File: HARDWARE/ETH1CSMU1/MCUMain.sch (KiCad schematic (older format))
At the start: 31 parts, among them J701 Conn_02x05, U701 STM32F746ZETx, U702 24LC08, X701 CRYSTAL_4PIN

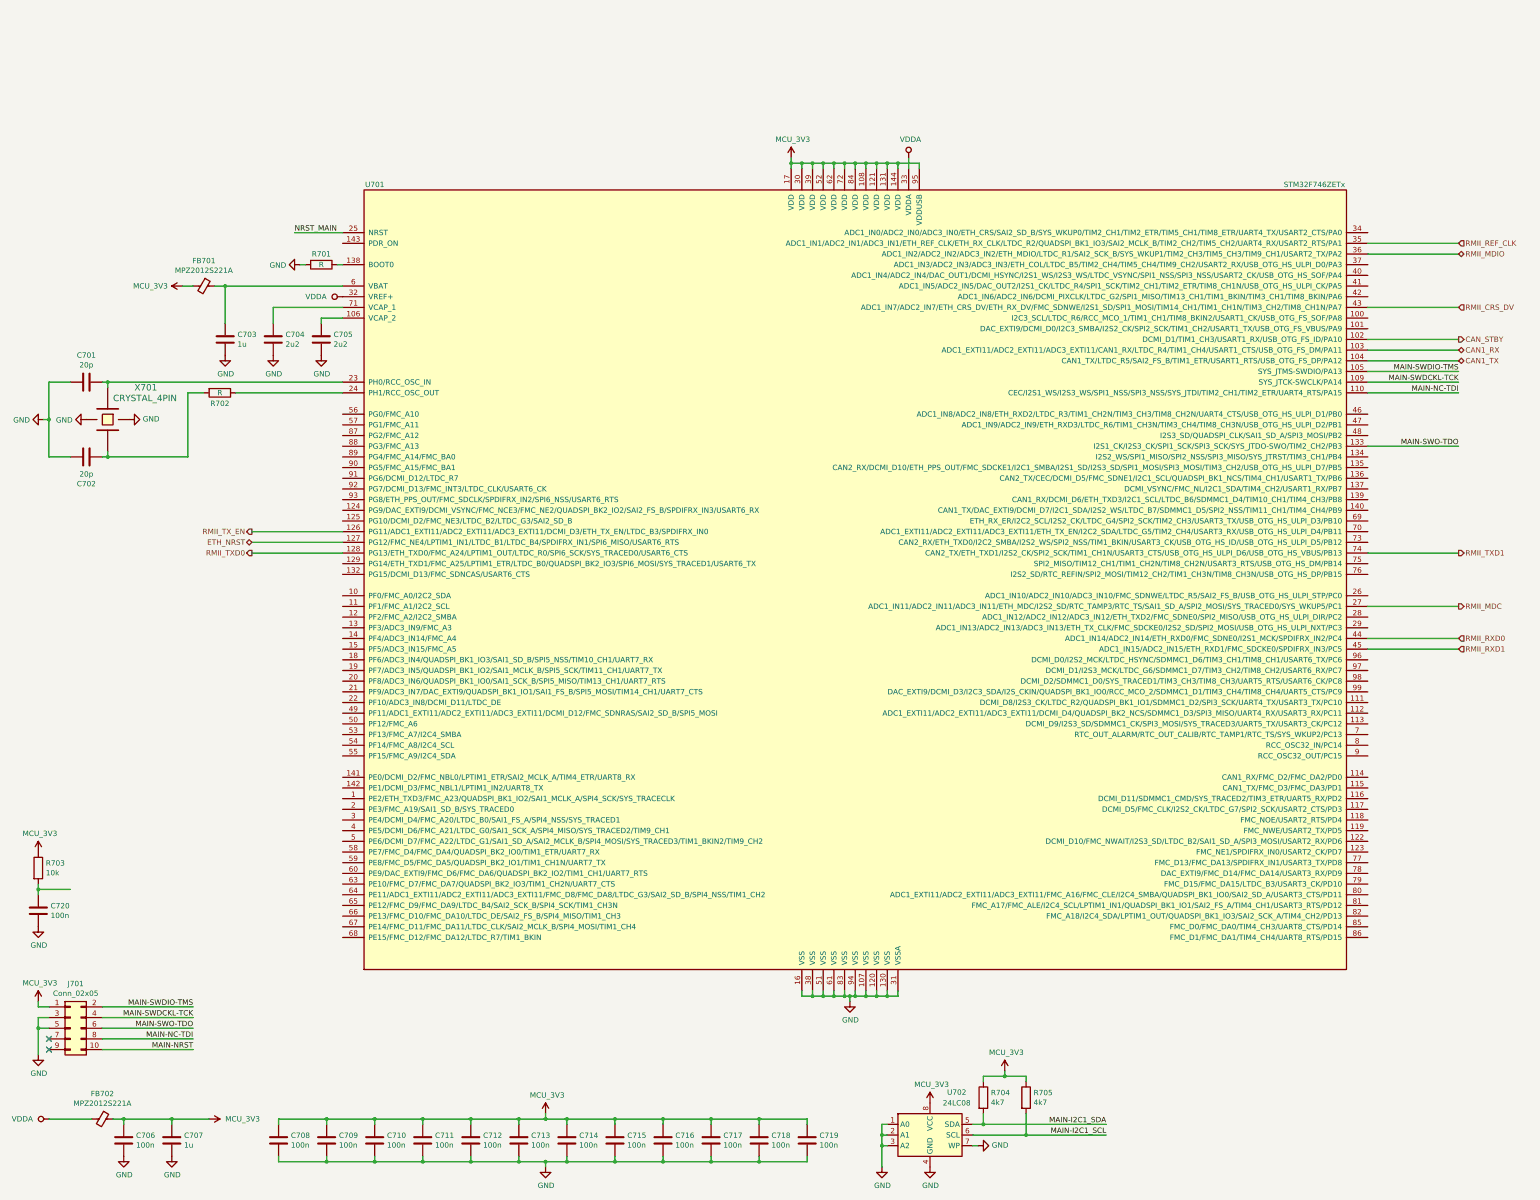
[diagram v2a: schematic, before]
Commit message: Power schematic
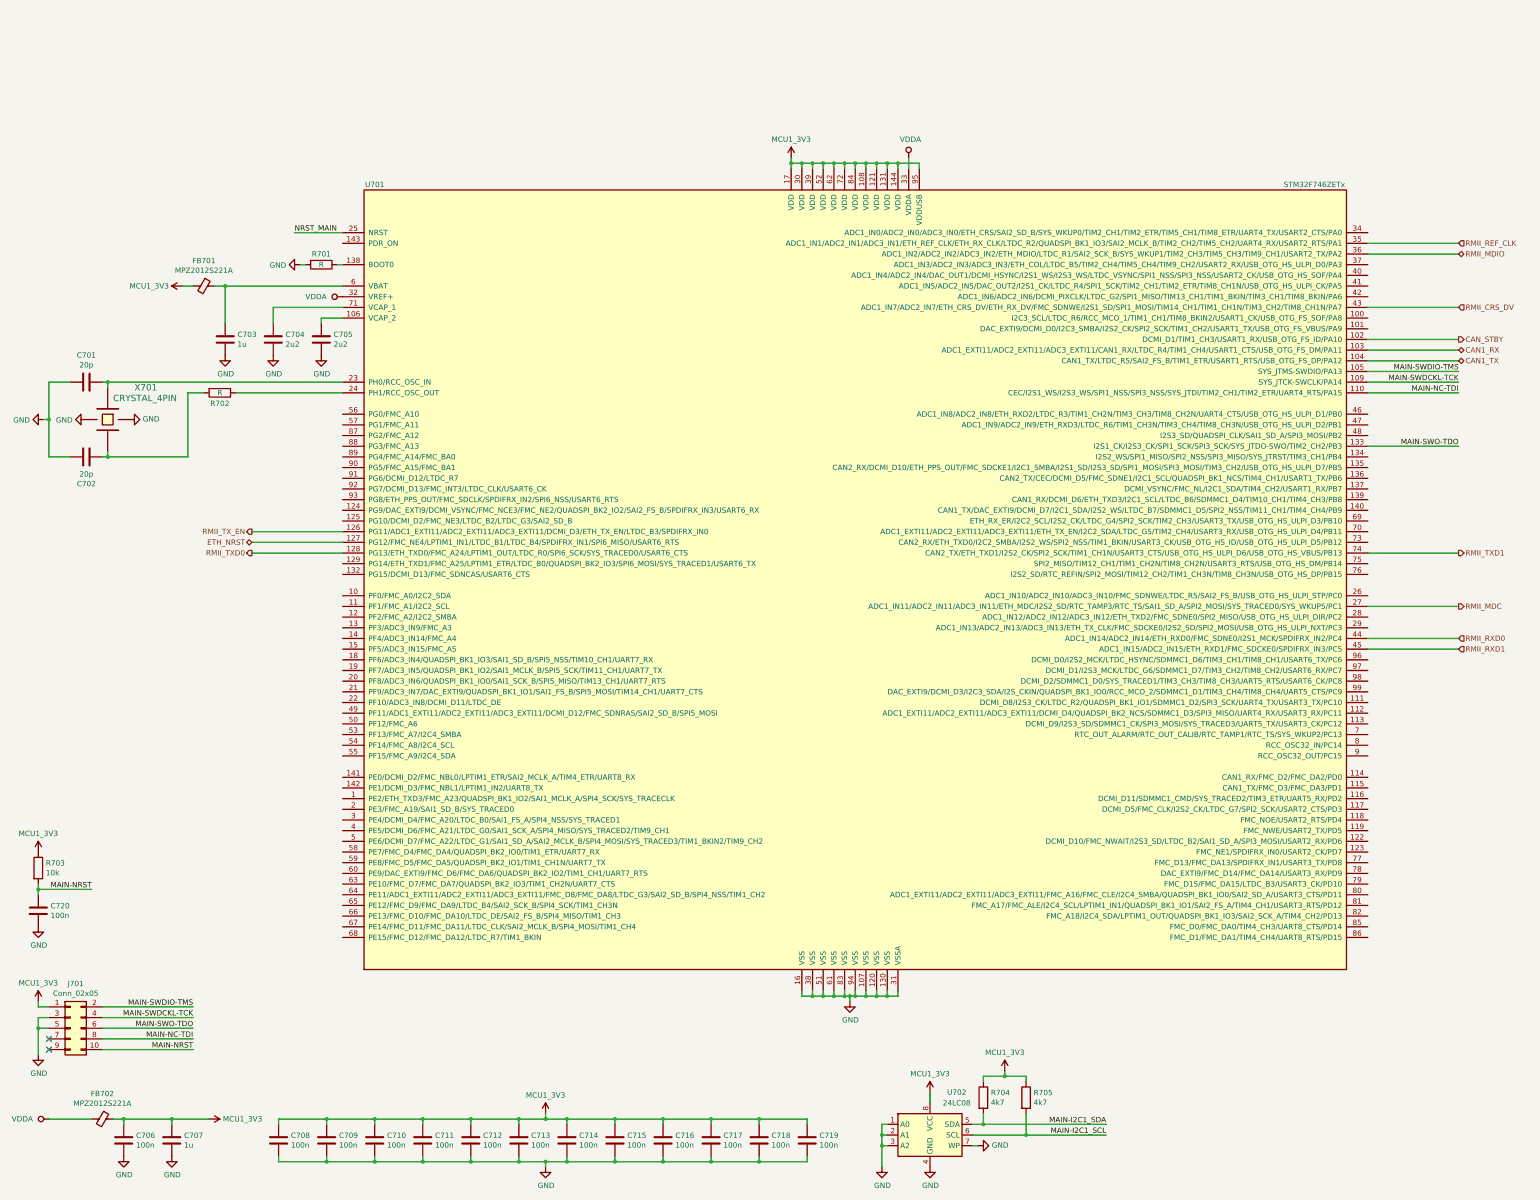
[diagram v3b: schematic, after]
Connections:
- net MAIN-NRST: now also C720.1, R703.2
- net MCU_3V3 renamed MCU1_3V3
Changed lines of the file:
@@
 $Descr A3 16535 11693
 encoding utf-8
-Sheet 7 12
+Sheet 7 13
 Title ""
 Date ""
@@
 F 3 "http://www.st.com/st-web-ui/static/active/en/resource/technical/document/datasheet/DM00166116.pdf" H 8450 5500 50  0001 C CNN
 	1    8450 5500
-	1    0    0    -1
-$EndComp
-$Comp
-L power_local:MCU_3V3 #PWR0702
-U 1 1 5BE1264D
-P 7850 1500
-F 0 "#PWR0702" H 7850 1350 50  0001 C CNN
-F 1 "MCU_3V3" H 7865 1673 50  0000 C CNN
-F 2 "" H 7850 1500 50  0000 C CNN
-F 3 "" H 7850 1500 50  0000 C CNN
-	1    7850 1500
 	1    0    0    -1
 $EndComp
@@
 Connection ~ 8850 1550
 $Comp
-L power_local:MCU_3V3 #PWR0703
-U 1 1 5BEBBE17
-P 2150 2700
-F 0 "#PWR0703" H 2150 2550 50  0001 C CNN
-F 1 "MCU_3V3" V 2150 3000 50  0000 C CNN
-F 2 "" H 2150 2700 50  0000 C CNN
-F 3 "" H 2150 2700 50  0000 C CNN
-	1    2150 2700
-	0    -1   -1   0
-$EndComp
-$Comp
 L Device:C C703
 U 1 1 5BEBD2EF
@@
 Connection ~ 2050 10500
 $Comp
-L power_local:MCU_3V3 #PWR0711
-U 1 1 5BEE572D
-P 2400 10500
-F 0 "#PWR0711" H 2400 10350 50  0001 C CNN
-F 1 "MCU_3V3" V 2400 10650 50  0000 L CNN
-F 2 "" H 2400 10500 50  0000 C CNN
-F 3 "" H 2400 10500 50  0000 C CNN
-	1    2400 10500
-	0    1    1    0
-$EndComp
-$Comp
 L power:VDDA #PWR0712
 U 1 1 5BEE8DB0
@@
 Wire Wire Line
 	5550 10900 5300 10900
-$Comp
-L power_local:MCU_3V3 #PWR0714
-U 1 1 5BF46B64
-P 5550 10450
-F 0 "#PWR0714" H 5550 10300 50  0001 C CNN
-F 1 "MCU_3V3" H 5565 10623 50  0000 C CNN
-F 2 "" H 5550 10450 50  0000 C CNN
-F 3 "" H 5550 10450 50  0000 C CNN
-	1    5550 10450
-	1    0    0    -1
-$EndComp
 Wire Wire Line
 	5550 10450 5550 10500
@@
 	1    0    0    -1
 $EndComp
-Wire Wire Line
-	800  8350 1100 8350
-$Comp
-L power_local:MCU_3V3 #PWR?
-U 1 1 5C07DDC6
-P 800 8000
-AR Path="/5BE0F4FE/5C07DDC6" Ref="#PWR?"  Part="1"
-AR Path="/5BE4235D/5C07DDC6" Ref="#PWR0716"  Part="1"
-F 0 "#PWR0716" H 800 7850 50  0001 C CNN
-F 1 "MCU_3V3" H 815 8173 50  0000 C CNN
-F 2 "" H 800 8000 50  0000 C CNN
-F 3 "" H 800 8000 50  0000 C CNN
-	1    800  8000
-	1    0    0    -1
-$EndComp
 $Comp
 L Connector_Generic:Conn_02x05_Odd_Even J?
@@
 F 3 "" H 800 9900 50  0001 C CNN
 	1    800  9900
-	1    0    0    -1
-$EndComp
-$Comp
-L power_local:MCU_3V3 #PWR?
-U 1 1 5BF91DF4
-P 800 9400
-AR Path="/5BE0F4FE/5BF91DF4" Ref="#PWR?"  Part="1"
-AR Path="/5BE4235D/5BF91DF4" Ref="#PWR0718"  Part="1"
-F 0 "#PWR0718" H 800 9250 50  0001 C CNN
-F 1 "MCU_3V3" H 815 9573 50  0000 C CNN
-F 2 "" H 800 9400 50  0000 C CNN
-F 3 "" H 800 9400 50  0000 C CNN
-	1    800  9400
 	1    0    0    -1
 $EndComp
@@
 	0    -1   -1   0
 $EndComp
-$Comp
-L power_local:MCU_3V3 #PWR?
-U 1 1 5C0622E5
-P 9150 10350
-AR Path="/5BE0F4FE/5C0622E5" Ref="#PWR?"  Part="1"
-AR Path="/5BE4235D/5C0622E5" Ref="#PWR0721"  Part="1"
-F 0 "#PWR0721" H 9150 10200 50  0001 C CNN
-F 1 "MCU_3V3" H 9165 10523 50  0000 C CNN
-F 2 "" H 9150 10350 50  0000 C CNN
-F 3 "" H 9150 10350 50  0000 C CNN
-	1    9150 10350
-	1    0    0    -1
-$EndComp
-$Comp
-L power_local:MCU_3V3 #PWR?
-U 1 1 5C0622EB
-P 9850 10050
-AR Path="/5BE0F4FE/5C0622EB" Ref="#PWR?"  Part="1"
-AR Path="/5BE4235D/5C0622EB" Ref="#PWR0724"  Part="1"
-F 0 "#PWR0724" H 9850 9900 50  0001 C CNN
-F 1 "MCU_3V3" H 9865 10223 50  0000 C CNN
-F 2 "" H 9850 10050 50  0000 C CNN
-F 3 "" H 9850 10050 50  0000 C CNN
-	1    9850 10050
-	1    0    0    -1
-$EndComp
 Wire Wire Line
 	2650 3700 3650 3700
@@
 Text HLabel 14100 3200 2    50   Output ~ 0
 CAN_STBY
+Text Label 1300 8350 2    50   ~ 0
+MAIN-NRST
+Wire Wire Line
+	800  8350 1300 8350
+$Comp
+L power_local:MCU1_3V3 #PWR?
+U 1 1 5C41AD37
+P 800 8000
+F 0 "#PWR?" H 800 7900 50  0001 C CNN
+F 1 "MCU1_3V3" H 800 8173 50  0000 C CNN
+F 2 "" H 800 8000 50  0000 C CNN
+F 3 "" H 800 8000 50  0000 C CNN
+	1    800  8000
+	1    0    0    -1
+$EndComp
+$Comp
+L power_local:MCU1_3V3 #PWR?
+U 1 1 5C41AE03
+P 800 9400
+F 0 "#PWR?" H 800 9300 50  0001 C CNN
+F 1 "MCU1_3V3" H 800 9573 50  0000 C CNN
+F 2 "" H 800 9400 50  0000 C CNN
+F 3 "" H 800 9400 50  0000 C CNN
+	1    800  9400
+	1    0    0    -1
+$EndComp
+$Comp
+L power_local:MCU1_3V3 #PWR?
+U 1 1 5C41AF63
+P 5550 10450
+F 0 "#PWR?" H 5550 10350 50  0001 C CNN
+F 1 "MCU1_3V3" H 5550 10623 50  0000 C CNN
+F 2 "" H 5550 10450 50  0000 C CNN
+F 3 "" H 5550 10450 50  0000 C CNN
+	1    5550 10450
+	1    0    0    -1
+$EndComp
+$Comp
+L power_local:MCU1_3V3 #PWR?
+U 1 1 5C41B120
+P 9850 10050
+F 0 "#PWR?" H 9850 9950 50  0001 C CNN
+F 1 "MCU1_3V3" H 9850 10223 50  0000 C CNN
+F 2 "" H 9850 10050 50  0000 C CNN
+F 3 "" H 9850 10050 50  0000 C CNN
+	1    9850 10050
+	1    0    0    -1
+$EndComp
+$Comp
+L power_local:MCU1_3V3 #PWR?
+U 1 1 5C41B280
+P 7850 1500
+F 0 "#PWR?" H 7850 1400 50  0001 C CNN
+F 1 "MCU1_3V3" H 7850 1673 50  0000 C CNN
+F 2 "" H 7850 1500 50  0000 C CNN
+F 3 "" H 7850 1500 50  0000 C CNN
+	1    7850 1500
+	1    0    0    -1
+$EndComp
+$Comp
+L power_local:MCU1_3V3 #PWR?
+U 1 1 5C41B516
+P 2150 2700
+F 0 "#PWR?" H 2150 2600 50  0001 C CNN
+F 1 "MCU1_3V3" V 2150 2827 50  0000 L CNN
+F 2 "" H 2150 2700 50  0000 C CNN
+F 3 "" H 2150 2700 50  0000 C CNN
+	1    2150 2700
+	0    -1   -1   0
+$EndComp
+$Comp
+L power_local:MCU1_3V3 #PWR?
+U 1 1 5C41D671
+P 9150 10250
+F 0 "#PWR?" H 9150 10150 50  0001 C CNN
+F 1 "MCU1_3V3" H 9150 10423 50  0000 C CNN
+F 2 "" H 9150 10250 50  0000 C CNN
+F 3 "" H 9150 10250 50  0000 C CNN
+	1    9150 10250
+	1    0    0    -1
+$EndComp
+Wire Wire Line
+	9150 10250 9150 10350
+$Comp
+L power_local:MCU1_3V3 #PWR?
+U 1 1 5C4345B7
+P 2400 10500
+F 0 "#PWR?" H 2400 10400 50  0001 C CNN
+F 1 "MCU1_3V3" V 2400 10628 50  0000 L CNN
+F 2 "" H 2400 10500 50  0000 C CNN
+F 3 "" H 2400 10500 50  0000 C CNN
+	1    2400 10500
+	0    1    1    0
+$EndComp
 $EndSCHEMATC

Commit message: Footprints
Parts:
- C701, C702: footprint (none) -> Capacitors_SMD:C_0603
- C706: footprint (none) -> SMD:C_0603_Symbol1
- J701: footprint (none) -> Pin_Headers:Pin_Header_Straight_2x05_Pitch1.27mm
- U701: footprint (none) -> SMD:TQFP-144
- U702: footprint (none) -> Housings_SSOP:MSOP-8_3x3mm_Pitch0.65mm
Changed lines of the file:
@@
 F 0 "U701" H 3950 9250 50  0000 C CNN
 F 1 "STM32F746ZETx" H 12750 9250 50  0000 C CNN
-F 2 "" H 13050 9175 50  0001 R TNN
+F 2 "SMD:TQFP-144" H 13050 9175 50  0001 R TNN
 F 3 "http://www.st.com/st-web-ui/static/active/en/resource/technical/document/datasheet/DM00166116.pdf" H 8450 5500 50  0001 C CNN
 	1    8450 5500
@@
 F 0 "C701" V 998 3600 50  0000 C CNN
 F 1 "20p" V 1089 3600 50  0000 C CNN
-F 2 "" H 1288 3450 50  0001 C CNN
+F 2 "Capacitors_SMD:C_0603" H 1288 3450 50  0001 C CNN
 F 3 "~" H 1250 3600 50  0001 C CNN
 	1    1250 3600
@@
 F 0 "C702" V 1502 4300 50  0000 C CNN
 F 1 "20p" V 1411 4300 50  0000 C CNN
-F 2 "" H 1288 4150 50  0001 C CNN
+F 2 "Capacitors_SMD:C_0603" H 1288 4150 50  0001 C CNN
 F 3 "~" H 1250 4300 50  0001 C CNN
 	1    1250 4300
@@
 F 0 "C706" H 1715 10746 50  0000 L CNN
 F 1 "100n" H 1715 10655 50  0000 L CNN
-F 2 "" H 1638 10550 50  0001 C CNN
+F 2 "SMD:C_0603_Symbol1" H 1638 10550 50  0001 C CNN
 F 3 "~" H 1600 10700 50  0001 C CNN
 	1    1600 10700
@@
 F 0 "J701" H 1150 10067 50  0000 C CNN
 F 1 "Conn_02x05" H 1150 9976 50  0000 C CNN
-F 2 "" H 1100 9650 50  0001 C CNN
+F 2 "Pin_Headers:Pin_Header_Straight_2x05_Pitch1.27mm" H 1100 9650 50  0001 C CNN
 F 3 "~" H 1100 9650 50  0001 C CNN
 	1    1100 9650
@@
 F 0 "U702" H 9400 11050 50  0000 C CNN
 F 1 "24LC08" H 9400 10950 50  0000 C CNN
-F 2 "" H 9150 10650 50  0001 C CNN
+F 2 "Housings_SSOP:MSOP-8_3x3mm_Pitch0.65mm" H 9150 10650 50  0001 C CNN
 F 3 "http://ww1.microchip.com/downloads/en/DeviceDoc/21710J.pdf" H 9150 10650 50  0001 C CNN
 	1    9150 10650
@@
 	800  8350 1300 8350
 $Comp
-L power_local:MCU1_3V3 #PWR?
+L power_local:MCU1_3V3 #PWR0123
 U 1 1 5C41AD37
 P 800 8000
-F 0 "#PWR?" H 800 7900 50  0001 C CNN
+F 0 "#PWR0123" H 800 7900 50  0001 C CNN
 F 1 "MCU1_3V3" H 800 8173 50  0000 C CNN
 F 2 "" H 800 8000 50  0000 C CNN
@@
 $EndComp
 $Comp
-L power_local:MCU1_3V3 #PWR?
+L power_local:MCU1_3V3 #PWR0124
 U 1 1 5C41AE03
 P 800 9400
-F 0 "#PWR?" H 800 9300 50  0001 C CNN
+F 0 "#PWR0124" H 800 9300 50  0001 C CNN
 F 1 "MCU1_3V3" H 800 9573 50  0000 C CNN
 F 2 "" H 800 9400 50  0000 C CNN
@@
 $EndComp
 $Comp
-L power_local:MCU1_3V3 #PWR?
+L power_local:MCU1_3V3 #PWR0125
 U 1 1 5C41AF63
 P 5550 10450
-F 0 "#PWR?" H 5550 10350 50  0001 C CNN
+F 0 "#PWR0125" H 5550 10350 50  0001 C CNN
 F 1 "MCU1_3V3" H 5550 10623 50  0000 C CNN
 F 2 "" H 5550 10450 50  0000 C CNN
@@
 $EndComp
 $Comp
-L power_local:MCU1_3V3 #PWR?
+L power_local:MCU1_3V3 #PWR0126
 U 1 1 5C41B120
 P 9850 10050
-F 0 "#PWR?" H 9850 9950 50  0001 C CNN
+F 0 "#PWR0126" H 9850 9950 50  0001 C CNN
 F 1 "MCU1_3V3" H 9850 10223 50  0000 C CNN
 F 2 "" H 9850 10050 50  0000 C CNN
@@
 $EndComp
 $Comp
-L power_local:MCU1_3V3 #PWR?
+L power_local:MCU1_3V3 #PWR0127
 U 1 1 5C41B280
 P 7850 1500
-F 0 "#PWR?" H 7850 1400 50  0001 C CNN
+F 0 "#PWR0127" H 7850 1400 50  0001 C CNN
 F 1 "MCU1_3V3" H 7850 1673 50  0000 C CNN
 F 2 "" H 7850 1500 50  0000 C CNN
@@
 $EndComp
 $Comp
-L power_local:MCU1_3V3 #PWR?
+L power_local:MCU1_3V3 #PWR0128
 U 1 1 5C41B516
 P 2150 2700
-F 0 "#PWR?" H 2150 2600 50  0001 C CNN
+F 0 "#PWR0128" H 2150 2600 50  0001 C CNN
 F 1 "MCU1_3V3" V 2150 2827 50  0000 L CNN
 F 2 "" H 2150 2700 50  0000 C CNN
@@
 $EndComp
 $Comp
-L power_local:MCU1_3V3 #PWR?
+L power_local:MCU1_3V3 #PWR0129
 U 1 1 5C41D671
 P 9150 10250
-F 0 "#PWR?" H 9150 10150 50  0001 C CNN
+F 0 "#PWR0129" H 9150 10150 50  0001 C CNN
 F 1 "MCU1_3V3" H 9150 10423 50  0000 C CNN
 F 2 "" H 9150 10250 50  0000 C CNN
@@
 	9150 10250 9150 10350
 $Comp
-L power_local:MCU1_3V3 #PWR?
+L power_local:MCU1_3V3 #PWR0130
 U 1 1 5C4345B7
 P 2400 10500
-F 0 "#PWR?" H 2400 10400 50  0001 C CNN
+F 0 "#PWR0130" H 2400 10400 50  0001 C CNN
 F 1 "MCU1_3V3" V 2400 10628 50  0000 L CNN
 F 2 "" H 2400 10500 50  0000 C CNN

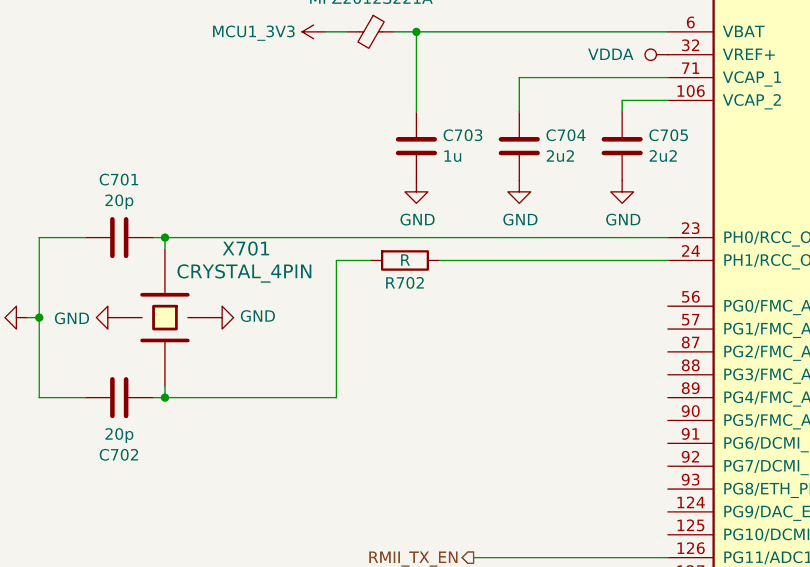
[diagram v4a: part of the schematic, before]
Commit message: Footprint selection
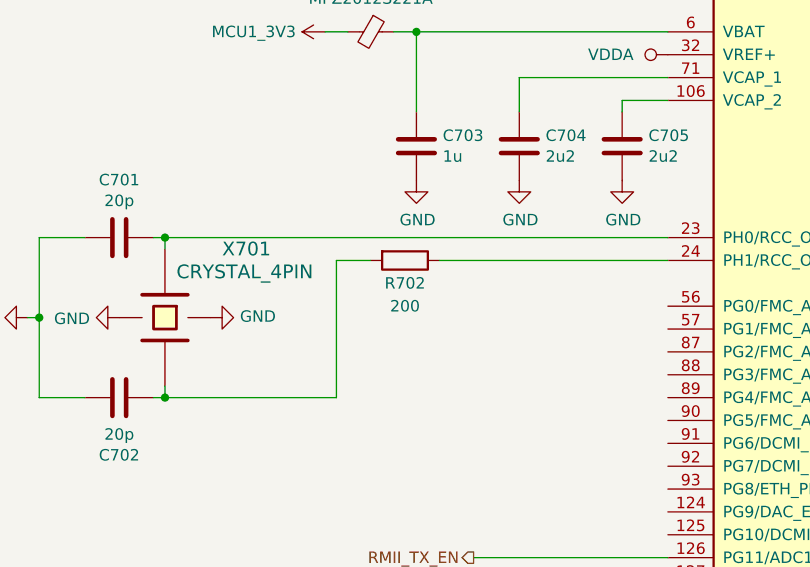
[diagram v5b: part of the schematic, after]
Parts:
- R702: value R -> 200
- R704, R705: footprint (none) -> SMD:R_0603_Symbol6
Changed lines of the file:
@@
 P 2500 3700
 F 0 "R702" V 2600 3700 50  0000 C CNN
-F 1 "R" V 2500 3700 50  0000 C CNN
+F 1 "200" V 2700 3700 50  0000 C CNN
 F 2 "" V 2430 3700 50  0001 C CNN
 F 3 "~" H 2500 3700 50  0001 C CNN
@@
 F 0 "R704" H 9720 10346 50  0000 L CNN
 F 1 "4k7" H 9720 10255 50  0000 L CNN
-F 2 "" V 9580 10300 50  0001 C CNN
+F 2 "SMD:R_0603_Symbol6" V 9580 10300 50  0001 C CNN
 F 3 "~" H 9650 10300 50  0001 C CNN
 	1    9650 10300
@@
 F 0 "R705" H 10120 10346 50  0000 L CNN
 F 1 "4k7" H 10120 10255 50  0000 L CNN
-F 2 "" V 9980 10300 50  0001 C CNN
+F 2 "SMD:R_0603_Symbol6" V 9980 10300 50  0001 C CNN
 F 3 "~" H 10050 10300 50  0001 C CNN
 	1    10050 10300
